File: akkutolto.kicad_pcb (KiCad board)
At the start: 2 copper layers, 33.8 x 43.5 mm, 13 parts, among them U1 LM317_TO-220, U2 LM317_TO-220

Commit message: Huzzad Pali
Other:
- board text added: "Akkutolto de HA6GBN"
- board text removed: "Akkutöltő de HA6GBN"
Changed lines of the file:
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@@
 		(layer "Edge.Cuts")
 	)
-	(gr_text "Akkutöltő \nde HA6GBN"
-		(at 100.05 109.05 0)
-		(layer "F.Cu" knockout)
+	(gr_text "Akkutolto de HA6GBN"
+		(at 98.171 105.791 0)
+		(layer "F.SilkS")
 		(effects
 			(font
-				(size 1.5 1.5)
-				(thickness 0.3)
+				(size 1 1)
+				(thickness 0.2)
 				(bold yes)
 			)
-			(justify left bottom)
+			(justify left)
 		)
 	)

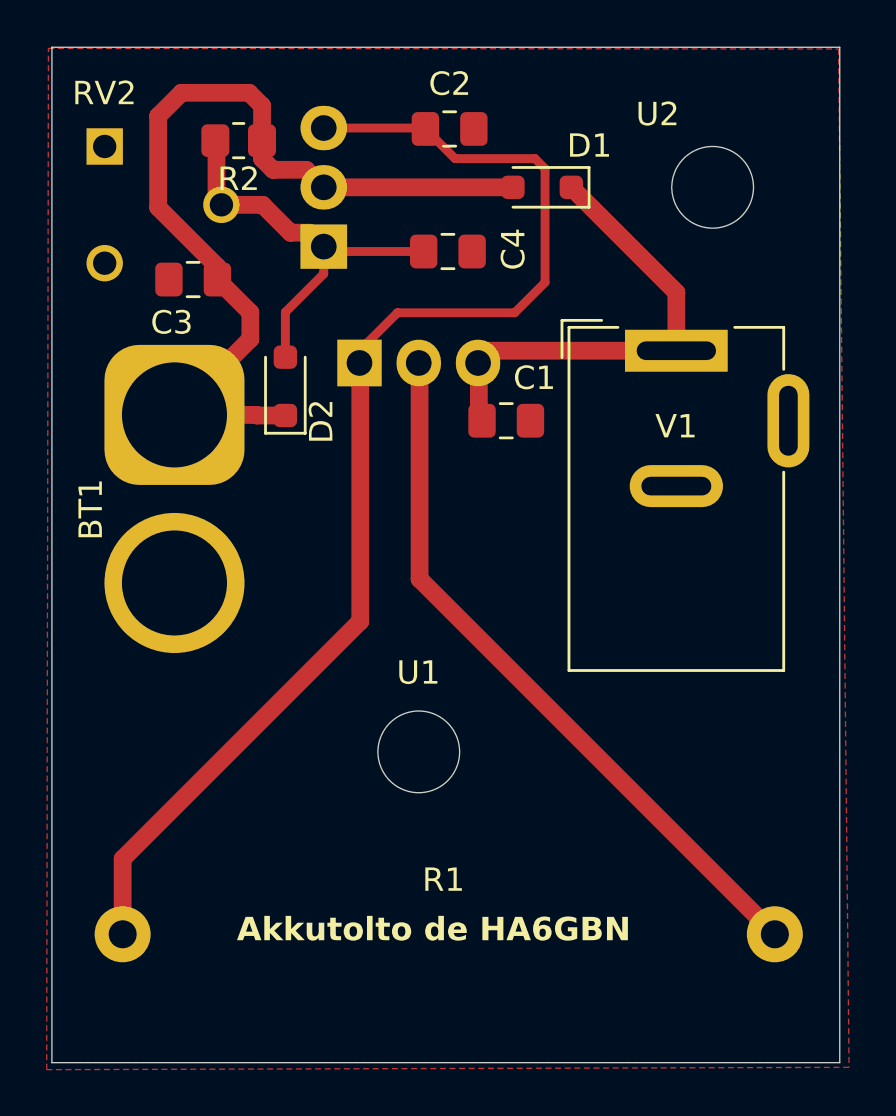
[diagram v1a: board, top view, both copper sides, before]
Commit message: Megvastagítottam pár nagyáramú vezetéket
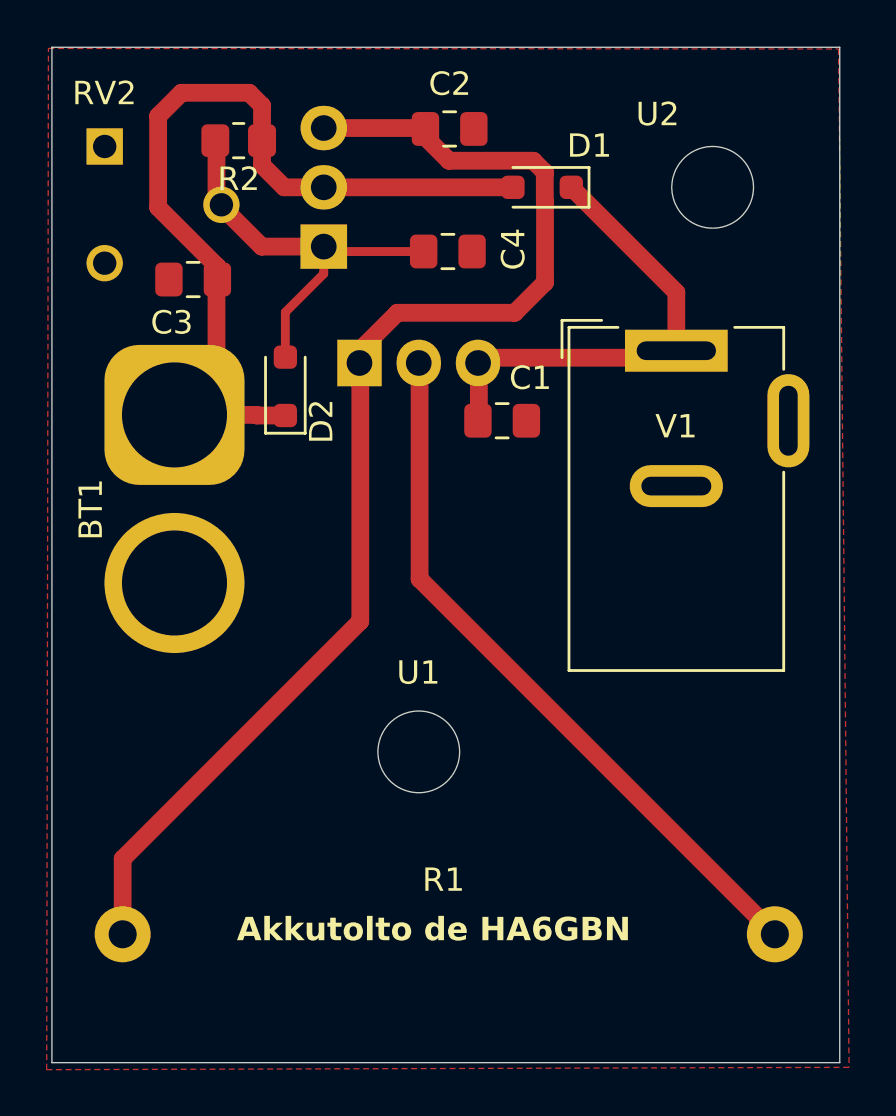
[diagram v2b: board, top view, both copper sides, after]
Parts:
- moved C1 0.18 mm to (109.5, 84.0)
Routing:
- net /out: track 39.2 -> 38.2 mm
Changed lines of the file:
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@@
 	(footprint "Capacitor_SMD:C_0805_2012Metric_Pad1.18x1.45mm_HandSolder"
 		(layer "F.Cu")
-		(at 109.7125 84)
+		(at 109.5375 84)
 		(descr "Capacitor SMD 0805 (2012 Metric), square (rectangular) end terminal, IPC-7351 nominal with elongated pad for handsoldering. (Body size source: IPC-SM-782 page 76, https://www.pcb-3d.com/wordpress/wp-content/uploads/ipc-sm-782a_amendment_1_and_2.pdf, https://docs.google.com/spreadsheets/d/1BsfQQcO9C6DZCsRaXUlFlo91Tg2WpOkGARC1WS5S8t0/edit?usp=sharing), generated with kicad-footprint-generator")
 		(tags "capacitor handsolder")
@@
 	)
 	(segment
+		(start 97.3 81.95)
+		(end 97.3 77.9875)
+		(width 0.762)
+		(layer "F.Cu")
+		(net 1)
+	)
+	(segment
 		(start 99.025 83.775)
 		(end 100.25 83.775)
@@
 	)
 	(segment
-		(start 98.75 79.3625)
+		(start 97.3 77.9875)
 		(end 97.3375 77.95)
-		(width 0.762)
-		(layer "F.Cu")
-		(net 1)
-	)
-	(segment
-		(start 99.25 72.775)
-		(end 99.725 73.25)
 		(width 0.762)
 		(layer "F.Cu")
@@
 	)
 	(segment
-		(start 101.145 73.25)
-		(end 101.895 74)
-		(width 0.762)
-		(layer "F.Cu")
-		(net 1)
-	)
-	(segment
 		(start 95.5 83.75)
-		(end 98.75 80.5)
+		(end 97.3 81.95)
 		(width 0.762)
 		(layer "F.Cu")
@@
 	)
 	(segment
-		(start 98.75 80.5)
-		(end 98.75 79.3625)
-		(width 0.762)
-		(layer "F.Cu")
-		(net 1)
-	)
-	(segment
 		(start 95.8 69.95)
 		(end 98.7 69.95)
@@
 	)
 	(segment
-		(start 99.725 73.25)
-		(end 101.145 73.25)
-		(width 0.762)
-		(layer "F.Cu")
-		(net 1)
-	)
-	(segment
 		(start 98.7 69.95)
 		(end 99.25 70.5)
@@
 	)
 	(segment
+		(start 100.2 74)
+		(end 101.895 74)
+		(width 0.762)
+		(layer "F.Cu")
+		(net 1)
+	)
+	(segment
+		(start 99.25 73.05)
+		(end 100.2 74)
+		(width 0.762)
+		(layer "F.Cu")
+		(net 1)
+	)
+	(segment
 		(start 99.25 72)
-		(end 99.25 72.775)
+		(end 99.25 73.05)
 		(width 0.762)
 		(layer "F.Cu")
 		(net 1)
+	)
+	(segment
+		(start 108.54 81.3)
+		(end 108.505 81.265)
+		(width 0.762)
+		(layer "F.Cu")
+		(net 3)
+	)
+	(segment
+		(start 117 81)
+		(end 116.7 81.3)
+		(width 0.762)
+		(layer "F.Cu")
+		(net 3)
 	)
 	(segment
@@
 	)
 	(segment
+		(start 108.505 81.265)
+		(end 108.505 81.525)
+		(width 0.762)
+		(layer "F.Cu")
+		(net 3)
+	)
+	(segment
 		(start 108.54 83.865)
 		(end 108.675 84)
@@
 	)
 	(segment
+		(start 116.7 81.3)
+		(end 108.54 81.3)
+		(width 0.762)
+		(layer "F.Cu")
+		(net 3)
+	)
+	(segment
 		(start 117 81)
 		(end 117 78.5)
@@
 	)
 	(segment
-		(start 108.505 81.265)
-		(end 108.505 81.525)
-		(width 0.762)
-		(layer "F.Cu")
-		(net 3)
-	)
-	(segment
-		(start 117 81)
-		(end 108.77 81)
-		(width 0.762)
-		(layer "F.Cu")
-		(net 3)
-	)
-	(segment
 		(start 108.505 81.525)
 		(end 108.54 81.56)
@@
 	)
 	(segment
-		(start 108.77 81)
-		(end 108.505 81.265)
-		(width 0.762)
-		(layer "F.Cu")
-		(net 3)
-	)
-	(segment
-		(start 107.521 72.771)
-		(end 110.946 72.771)
-		(width 0.381)
+		(start 111.364 73.37608)
+		(end 111.364 74.62392)
+		(width 0.762)
 		(layer "F.Cu")
 		(net 4)
 	)
 	(segment
-		(start 111.375 73.2)
+		(start 111.375 74.63492)
 		(end 111.375 78.075)
-		(width 0.381)
+		(width 0.762)
 		(layer "F.Cu")
 		(net 4)
@@
 		(start 103.655 80.77)
 		(end 103.655 81.295)
-		(width 0.381)
+		(width 0.762)
 		(layer "F.Cu")
 		(net 4)
 	)
 	(segment
-		(start 110.946 72.771)
-		(end 111.375 73.2)
-		(width 0.381)
+		(start 105.05 79.375)
+		(end 103.655 80.77)
+		(width 0.762)
+		(layer "F.Cu")
+		(net 4)
+	)
+	(segment
+		(start 103.46 81.56)
+		(end 103.46 92.59)
+		(width 0.762)
+		(layer "F.Cu")
+		(net 4)
+	)
+	(segment
+		(start 103.425 81.525)
+		(end 103.46 81.56)
+		(width 0.762)
+		(layer "F.Cu")
+		(net 4)
+	)
+	(segment
+		(start 106.21 71.46)
+		(end 106.25 71.5)
+		(width 0.762)
+		(layer "F.Cu")
+		(net 4)
+	)
+	(segment
+		(start 106.25 71.85)
+		(end 107.261 72.861)
+		(width 0.762)
+		(layer "F.Cu")
+		(net 4)
+	)
+	(segment
+		(start 106.25 71.5)
+		(end 106.25 71.85)
+		(width 0.762)
+		(layer "F.Cu")
+		(net 4)
+	)
+	(segment
+		(start 111.375 73.36508)
+		(end 111.364 73.37608)
+		(width 0.762)
+		(layer "F.Cu")
+		(net 4)
+	)
+	(segment
+		(start 101.895 71.46)
+		(end 106.21 71.46)
+		(width 0.762)
 		(layer "F.Cu")
 		(net 4)
@@
 		(start 110.075 79.375)
 		(end 105.05 79.375)
-		(width 0.381)
+		(width 0.762)
 		(layer "F.Cu")
 		(net 4)
 	)
 	(segment
-		(start 103.46 81.56)
-		(end 103.46 92.59)
+		(start 107.261 72.861)
+		(end 110.87092 72.861)
 		(width 0.762)
 		(layer "F.Cu")
@@
 	)
 	(segment
-		(start 103.425 81.525)
-		(end 103.46 81.56)
+		(start 111.375 78.075)
+		(end 110.075 79.375)
 		(width 0.762)
 		(layer "F.Cu")
@@
 	)
 	(segment
-		(start 106.21 71.46)
-		(end 106.25 71.5)
-		(width 0.381)
+		(start 111.364 74.62392)
+		(end 111.375 74.63492)
+		(width 0.762)
 		(layer "F.Cu")
 		(net 4)
 	)
 	(segment
-		(start 105.05 79.375)
-		(end 103.655 80.77)
-		(width 0.381)
+		(start 103.46 92.59)
+		(end 93.28 102.77)
+		(width 0.762)
 		(layer "F.Cu")
 		(net 4)
 	)
 	(segment
-		(start 106.25 71.5)
-		(end 107.521 72.771)
-		(width 0.381)
+		(start 110.87092 72.861)
+		(end 111.375 73.36508)
+		(width 0.762)
 		(layer "F.Cu")
 		(net 4)
@@
 		(start 103.655 81.295)
 		(end 103.425 81.525)
-		(width 0.381)
-		(layer "F.Cu")
-		(net 4)
-	)
-	(segment
-		(start 101.895 71.46)
-		(end 106.21 71.46)
-		(width 0.381)
-		(layer "F.Cu")
-		(net 4)
-	)
-	(segment
-		(start 103.46 92.59)
-		(end 93.28 102.77)
-		(width 0.762)
-		(layer "F.Cu")
-		(net 4)
-	)
-	(segment
-		(start 111.375 78.075)
-		(end 110.075 79.375)
-		(width 0.381)
+		(width 0.762)
 		(layer "F.Cu")
 		(net 4)
@@
 	)
 	(segment
-		(start 100.468357 75.943357)
-		(end 99.275 74.75)
+		(start 99.24 76.54)
+		(end 97.51 74.81)
 		(width 0.762)
 		(layer "F.Cu")
@@
 	)
 	(segment
-		(start 101.895 76.54)
-		(end 101.298357 75.943357)
+		(start 97.51 74.81)
+		(end 97.51 74.75)
 		(width 0.762)
 		(layer "F.Cu")
@@
 	)
 	(segment
+		(start 101.895 76.54)
+		(end 99.24 76.54)
+		(width 0.762)
+		(layer "F.Cu")
+		(net 5)
+	)
+	(segment
 		(start 97.3 72.05)
 		(end 97.25 72)
 		(width 0.762)
 		(layer "F.Cu")
-		(net 5)
-	)
-	(segment
-		(start 101.298357 75.943357)
-		(end 100.468357 75.943357)
-		(width 0.762)
-		(layer "F.Cu")
-		(net 5)
-	)
-	(segment
-		(start 99.275 74.75)
-		(end 97.51 74.75)
-		(width 0.762)
-		(layer "F.Cu")
